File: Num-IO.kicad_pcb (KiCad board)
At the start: 2 copper layers, 170.2 x 61.1 mm, 123 parts, among them J1 DB37_Female, J2 DB37_Male, J3 Conn_02x25_Odd_Even, J4 0826-1X1T-GH-F, J5 Conn_01x02_Male, J6 Conn_01x02_Male, J7 Conn_01x02_Male, J8 Conn_01x02_Male, J9 Conn_01x02_Male, U1 MAX14917AFM+, U10 LTC6820HMS, U11 LTC6820HMS, U12 LTC6820HMS, U13 AP1117-33, U2 MAX14917AFM+, U3 MAX14851AEE+, U4 MAX14917AFM+, U5 MAX31910AUI+, U6 MAX31910AUI+, U7 MAX31910AUI+, U8 MAX31910AUI+, U9 LTC6820HMS

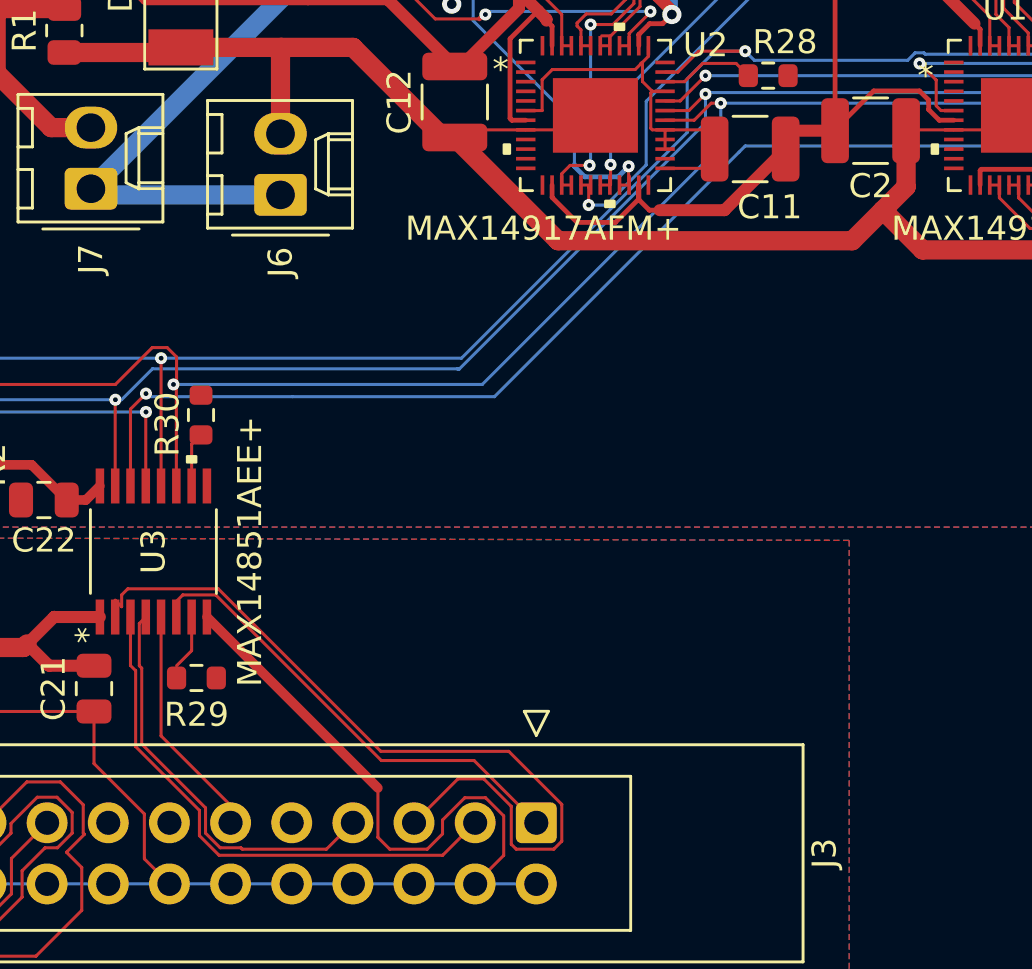
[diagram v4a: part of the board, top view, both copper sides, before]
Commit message: add resistances for bypassing the isolator
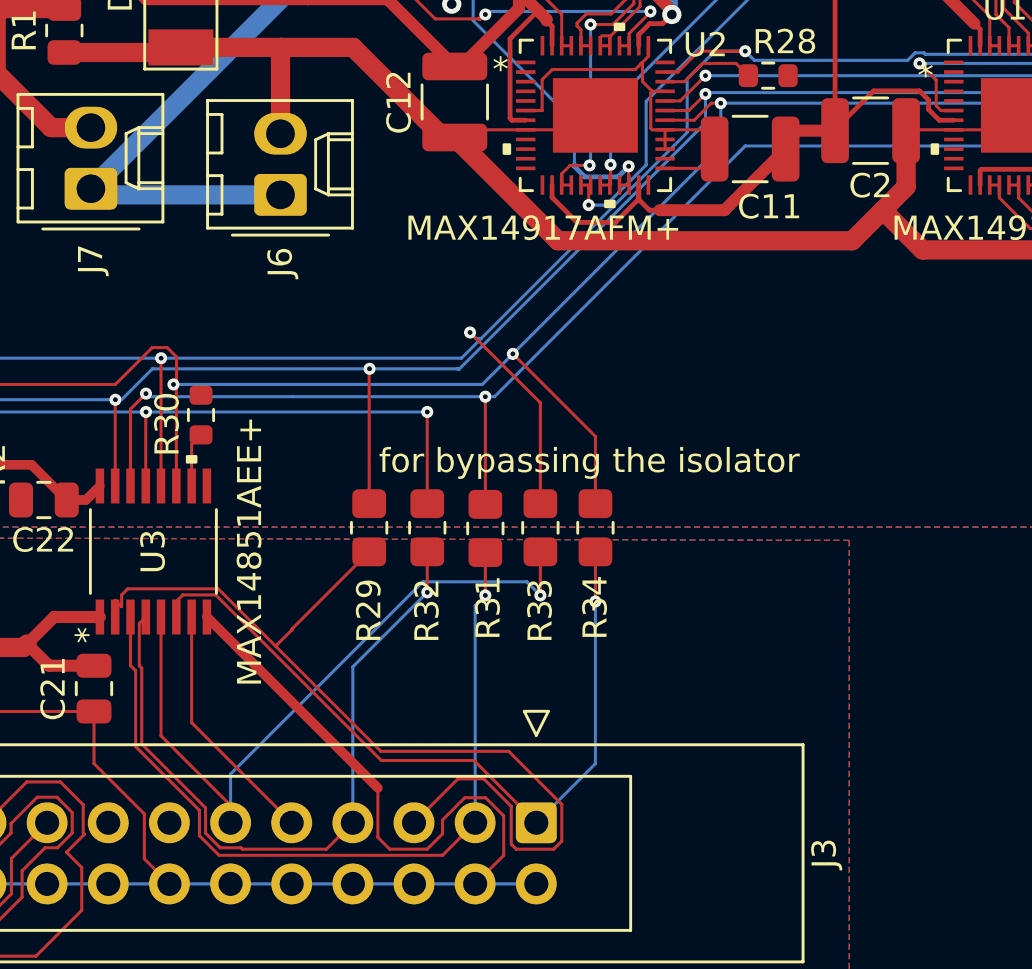
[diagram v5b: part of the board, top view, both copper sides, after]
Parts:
- added R31: NC, Resistor_SMD:R_0805_2012Metric_Pad1.20x1.40mm_HandSolder, F.Cu at (170.7, 63.5)
- added R32: NC, Resistor_SMD:R_0805_2012Metric_Pad1.20x1.40mm_HandSolder, F.Cu at (168.3, 63.5)
- added R33: NC, Resistor_SMD:R_0805_2012Metric_Pad1.20x1.40mm_HandSolder, F.Cu at (173.0, 63.5)
- added R34: NC, Resistor_SMD:R_0805_2012Metric_Pad1.20x1.40mm_HandSolder, F.Cu at (175.3, 63.5)
- R29: value 100k -> NC; footprint Resistor_SMD:R_0603_1608Metric -> Resistor_SMD:R_0805_2012Metric_Pad1.20x1.40mm_HandSolder
- moved R29 9.51 mm to (165.9, 63.5), turned to 90 degrees
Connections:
- J3 pad 9: /FPGA Connector/ADDR -> /IADDR
- R29 pad 1: Net-(U3-Pad7) -> /FPGA Connector/SPI0.CLK
- R29 pad 2: GNDD -> /CLK
- U3 pad 7: Net-(U3-Pad7) -> /IADDR
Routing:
- net /I*FAULT: track 9.74 -> 30.0 mm, vias 0 -> 1
- net /SDO: track 60.0 -> 75.5 mm, vias 2 -> 3
- net /FPGA Connector/SPI0.SDO: track 17.1 -> 29.6 mm, vias 0 -> 1
- net /FPGA Connector/SPI0.*CS: track 19.6 -> 31.9 mm, vias 0 -> 1
- net /FPGA Connector/SPI0.SDI: track 22.6 -> 34.0 mm, vias 0 -> 1
- net /IADDR: track 0.00 -> 10.3 mm
- net /*FAULT: track 148.8 -> 157.7 mm, vias 9 -> 10
- net /CS: track 143.0 -> 150.6 mm, vias 9 -> 10
- net /CLK: track 140.7 -> 146.3 mm, vias 8 -> 9
- net /FPGA Connector/SPI0.CLK: track 34.4 -> 39.9 mm
- net /SDI: track 72.7 -> 77.2 mm, vias 2 -> 3
- net Net-(U3-Pad7): track 2.28 -> 0.00 mm
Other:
- board text added: "for bypassing the isolator"
